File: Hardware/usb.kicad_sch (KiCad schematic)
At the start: 8 parts, among them J2 USB_C_Receptacle_USB2.0

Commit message: Crosshair V1.0
New pyro connectors, silkscreen sorted, mostly connected properly + cool new name and image
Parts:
- J2: footprint Connector_USB:USB_C_Receptacle_Palconn_UTC16-G -> iclr:USB_C_Receptacle_Palconn_UTC16-G
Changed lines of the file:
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@@
 (kicad_sch
-	(version 20231120)
+	(version 20250114)
 	(generator "eeschema")
-	(generator_version "8.0")
+	(generator_version "9.0")
 	(paper "A4")
 	(junction
@@
 	(label "Data+"
 		(at 134.62 134.62 90)
-		(fields_autoplaced yes)
 		(effects
 			(font
@@
 	(label "Data+"
 		(at 44.45 104.14 0)
-		(fields_autoplaced yes)
 		(effects
 			(font
@@
 	(label "Data-"
 		(at 44.45 99.06 0)
-		(fields_autoplaced yes)
 		(effects
 			(font
@@
 	(label "Data-"
 		(at 132.08 134.62 90)
-		(fields_autoplaced yes)
 		(effects
 			(font
@@
 	(label "Data-"
 		(at 116.84 102.87 0)
-		(fields_autoplaced yes)
 		(effects
 			(font
@@
 	(label "Data+"
 		(at 116.84 107.95 0)
-		(fields_autoplaced yes)
 		(effects
 			(font
@@
 		(shape bidirectional)
 		(at 44.45 99.06 180)
-		(fields_autoplaced yes)
 		(effects
 			(font
@@
 		(shape bidirectional)
 		(at 44.45 104.14 180)
-		(fields_autoplaced yes)
 		(effects
 			(font
@@
 			)
 		)
-		(property "Footprint" "Connector_USB:USB_C_Receptacle_Palconn_UTC16-G"
+		(property "Footprint" "iclr:USB_C_Receptacle_Palconn_UTC16-G"
 			(at 104.14 104.14 0)
 			(effects

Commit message: Mega commit
Post review changes
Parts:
- USBLED1: footprint Resistor_SMD:R_0402_1005Metric -> LED_SMD:LED_0402_1005Metric
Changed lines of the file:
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@@
 			)
 		)
-		(property "Footprint" "Resistor_SMD:R_0402_1005Metric"
+		(property "Footprint" "LED_SMD:LED_0402_1005Metric"
 			(at 162.56 92.71 90)
 			(effects

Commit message: V2 changes, post review work
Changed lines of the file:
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@@
+	(wire
+		(pts
+			(xy 168.91 92.71) (xy 165.1 92.71)
+		)
+		(stroke
+			(width 0)
+			(type default)
+		)
+	)
 	(wire
 		(pts
@@
 	(wire
 		(pts
+			(xy 148.59 92.71) (xy 152.4 92.71)
+		)
+		(stroke
+			(width 0)
+			(type default)
+		)
+	)
+	(wire
+		(pts
 			(xy 115.57 93.98) (xy 120.65 93.98)
 		)
@@
 	(wire
 		(pts
-			(xy 125.73 96.52) (xy 127 96.52)
+			(xy 125.73 96.52) (xy 134.62 96.52)
 		)
 		(stroke
@@
 	(symbol
 		(lib_id "power:GND")
-		(at 127 96.52 90)
+		(at 134.62 96.52 0)
 		(unit 1)
 		(exclude_from_sim no)
@@
 		(dnp no)
 		(property "Reference" "#PWR031"
-			(at 133.35 96.52 0)
+			(at 134.62 102.87 0)
 			(effects
 				(font
@@
 		)
 		(property "Value" "GND"
-			(at 130.2512 96.393 90)
+			(at 136.144 100.838 0)
 			(effects
 				(font
@@
 		)
 		(property "Footprint" ""
-			(at 127 96.52 0)
+			(at 134.62 96.52 0)
 			(effects
 				(font
@@
 		)
 		(property "Datasheet" ""
-			(at 127 96.52 0)
-			(effects
-				(font
-					(size 1.27 1.27)
-				)
-				(hide yes)
-			)
-		)
-		(property "Description" ""
-			(at 127 96.52 0)
+			(at 134.62 96.52 0)
+			(effects
+				(font
+					(size 1.27 1.27)
+				)
+				(hide yes)
+			)
+		)
+		(property "Description" ""
+			(at 134.62 96.52 0)
 			(effects
 				(font
@@
 		(dnp no)
 		(property "Reference" "R12"
-			(at 129.54 100.33 90)
+			(at 126.746 101.092 90)
 			(effects
 				(font
@@
 		)
 		(property "Value" "5.1k"
-			(at 129.54 102.6414 90)
+			(at 126.746 103.4034 90)
 			(effects
 				(font
@@
 		)
 		(property "Value" "VBUS"
-			(at 117.221 81.8388 90)
+			(at 114.554 81.026 0)
 			(effects
 				(font
@@
 	(symbol
 		(lib_id "power:GND")
-		(at 165.1 92.71 90)
+		(at 168.91 92.71 0)
 		(unit 1)
 		(exclude_from_sim no)
@@
 		(dnp no)
 		(property "Reference" "#PWR034"
-			(at 171.45 92.71 0)
+			(at 168.91 99.06 0)
 			(effects
 				(font
@@
 		)
 		(property "Value" "GND"
-			(at 168.3512 92.583 90)
+			(at 170.942 97.028 0)
 			(effects
 				(font
@@
 		)
 		(property "Footprint" ""
-			(at 165.1 92.71 0)
+			(at 168.91 92.71 0)
 			(effects
 				(font
@@
 		)
 		(property "Datasheet" ""
-			(at 165.1 92.71 0)
-			(effects
-				(font
-					(size 1.27 1.27)
-				)
-				(hide yes)
-			)
-		)
-		(property "Description" ""
-			(at 165.1 92.71 0)
+			(at 168.91 92.71 0)
+			(effects
+				(font
+					(size 1.27 1.27)
+				)
+				(hide yes)
+			)
+		)
+		(property "Description" ""
+			(at 168.91 92.71 0)
 			(effects
 				(font
@@
 	(symbol
 		(lib_id "power:VBUS")
-		(at 152.4 92.71 90)
+		(at 148.59 92.71 0)
 		(unit 1)
 		(exclude_from_sim no)
@@
 		(dnp no)
 		(property "Reference" "#PWR033"
-			(at 156.21 92.71 0)
+			(at 148.59 96.52 0)
 			(effects
 				(font
@@
 		)
 		(property "Value" "VBUS"
-			(at 149.1488 92.329 90)
+			(at 146.05 88.138 0)
 			(effects
 				(font
@@
 		)
 		(property "Footprint" ""
-			(at 152.4 92.71 0)
+			(at 148.59 92.71 0)
 			(effects
 				(font
@@
 		)
 		(property "Datasheet" ""
-			(at 152.4 92.71 0)
-			(effects
-				(font
-					(size 1.27 1.27)
-				)
-				(hide yes)
-			)
-		)
-		(property "Description" ""
-			(at 152.4 92.71 0)
-			(effects
-				(font
+			(at 148.59 92.71 0)
+			(effects
+				(font
+					(size 1.27 1.27)
+				)
+				(hide yes)
+			)
+		)
+		(property "Description" ""
+			(at 148.59 92.71 0)
+			(effects
+				(font

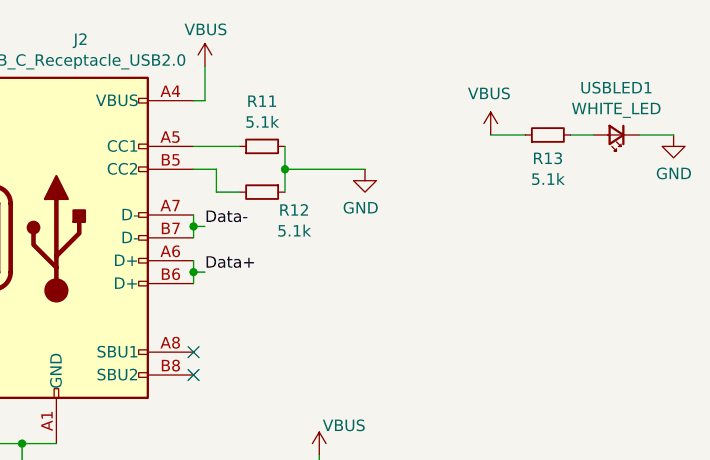
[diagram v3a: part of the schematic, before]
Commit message: More V2 changes
Mainly changed to use Ω symbol for resistors. Fixed the CDC pin for the buck boost
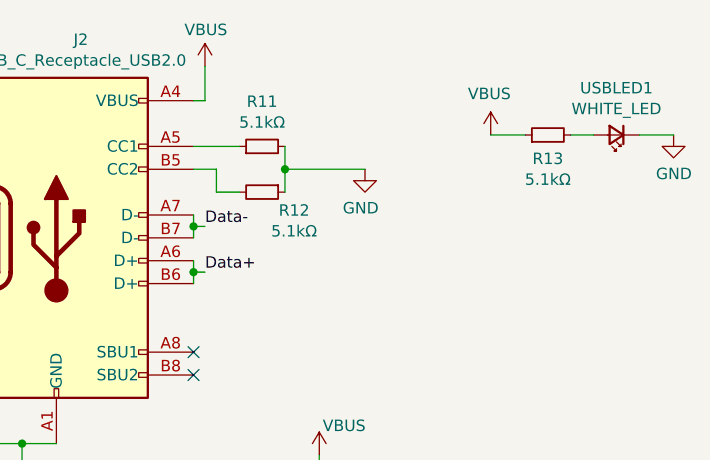
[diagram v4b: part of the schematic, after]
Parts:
- R11, R12, R13: value 5.1k -> 5.1kΩ
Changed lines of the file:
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@@
 			)
 		)
-		(property "Value" "5.1k"
+		(property "Value" "5.1kΩ"
 			(at 126.746 103.4034 90)
 			(effects
@@
 			)
 		)
-		(property "Value" "5.1k"
+		(property "Value" "5.1kΩ"
 			(at 123.19 91.313 90)
 			(effects
@@
 			)
 		)
-		(property "Value" "5.1k"
+		(property "Value" "5.1kΩ"
 			(at 154.94 97.663 90)
 			(effects

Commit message: reformatted and renamed file
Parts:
- D502: renamed from USBLED1; value WHITE_LED -> LED_WHITE
- TP501: renamed from TP1; now left out of the parts list
- TP502: renamed from TP2; now left out of the parts list
- renumbered D2 to D501, J2 to J501, R11 to R501, R12 to R502, R13 to R503
